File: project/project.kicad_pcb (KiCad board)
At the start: 2 copper layers, 20 x 30 mm, 10 parts, among them J1 flasher, U1 ESP32-WROOM-32

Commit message: marking version
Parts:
- removed kibuzzard-642C03EC: G***, kibuzzard-642C03EC
- added kibuzzard-64D00BC3: G***, kibuzzard-64D00BC3, F.Cu at (179.0, 116.0)

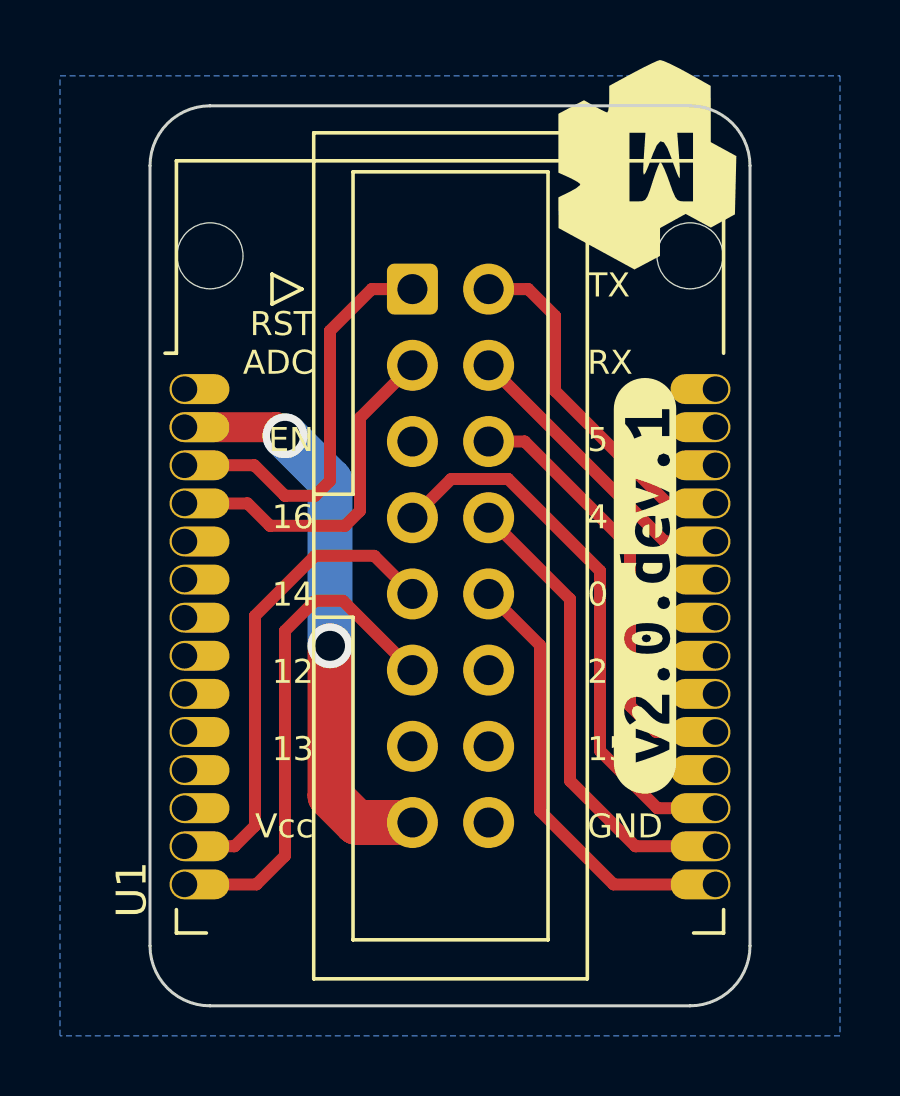
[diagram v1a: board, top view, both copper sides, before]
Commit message: using smaller 2x4 connector and shrinking pcb
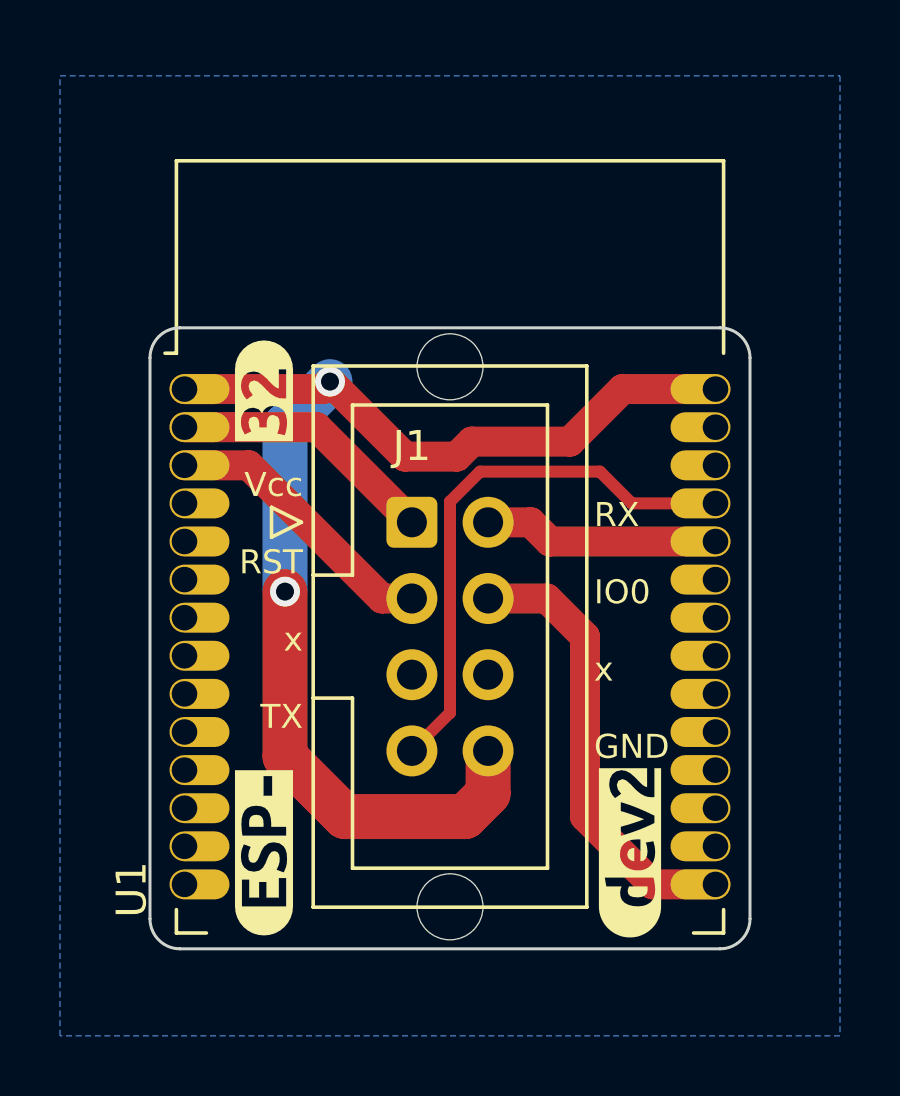
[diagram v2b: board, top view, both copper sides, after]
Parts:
- removed kibuzzard-64C972AC: G***, kibuzzard-64C972AC
- removed kibuzzard-64C97AAF: G***, kibuzzard-64C97AAF
- removed kibuzzard-64C97AF4: G***, kibuzzard-64C97AF4
- removed kibuzzard-64D00BC3: G***, kibuzzard-64D00BC3
- added kibuzzard-64DF42DF: G***, kibuzzard-64DF42DF, F.Cu at (166.3, 109.5)
- added kibuzzard-64DF42F1: G***, kibuzzard-64DF42F1, F.Cu at (166.3, 124.9)
- added kibuzzard-64DF4388: G***, kibuzzard-64DF4388, B.Cu at (177.9, 117.7)
- added kibuzzard-64DF4440: G***, kibuzzard-64DF4440, F.Cu at (178.5, 124.9)
- G2: moved to B.Cu
- J1: footprint Connector_IDC:IDC-Header_2x08_P2.54mm_Vertical -> Connector_IDC:IDC-Header_2x04_P2.54mm_Vertical
- moved G2 24.8 mm to (168.7, 124.3)
- moved REF** 23.1 mm to (172.5, 126.7)
- moved G1 16.1 mm to (168.7, 110.9)
- moved REF** 8.81 mm to (172.5, 108.7)
- moved J1 7.77 mm to (171.2, 113.9)
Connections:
- J1 pad 1: RST -> Vcc
- J1 pad 2: TX -> RX
- J1 pad 3: ADC -> RST
- J1 pad 4: RX -> IO0
- J1 pad 5: unconnected-(J1-Pad5) -> EN
- J1 pad 6: IO5 -> IO2
- J1 pad 7: IO16 -> TX
- J1 pad 8: IO4 -> GND
- U1 pad 13: IO14 -> unconnected-(U1-Pad13)
- U1 pad 14: IO12 -> unconnected-(U1-Pad14)
- U1 pad 26: IO4 -> unconnected-(U1-Pad26)
- U1 pad 27: IO16 -> unconnected-(U1-Pad27)
- U1 pad 29: IO5 -> unconnected-(U1-Pad29)
- U1 pad 4: ADC -> unconnected-(U1-Pad4)
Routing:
- net GND: track 0.00 -> 42.2 mm, vias 0 -> 2
- net IO16: track 18.7 -> 0.00 mm
- net IO12: track 16.9 -> 0.00 mm
- net IO14: track 16.2 -> 0.00 mm
- net IO4: track 15.6 -> 0.00 mm
- net IO5: track 14.7 -> 0.00 mm
- net ADC: track 11.9 -> 0.00 mm
- net Vcc: track 19.2 -> 8.89 mm, vias 2 -> 0
- net TX: track 12.0 -> 18.5 mm
- net RST: track 13.8 -> 9.42 mm
- net RX: track 9.99 -> 7.85 mm
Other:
- board size 20 x 30 mm -> 20 x 20.7 mm
- board text added: "RX IO0 x GND"
- board text added: "Vcc RST x TX"
- board text removed: "RST ADC EN 16 14 12 13 Vcc"
- board text removed: "TX RX 5 4 0 2 15 GND"

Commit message: adding 4 screwholes for mounting
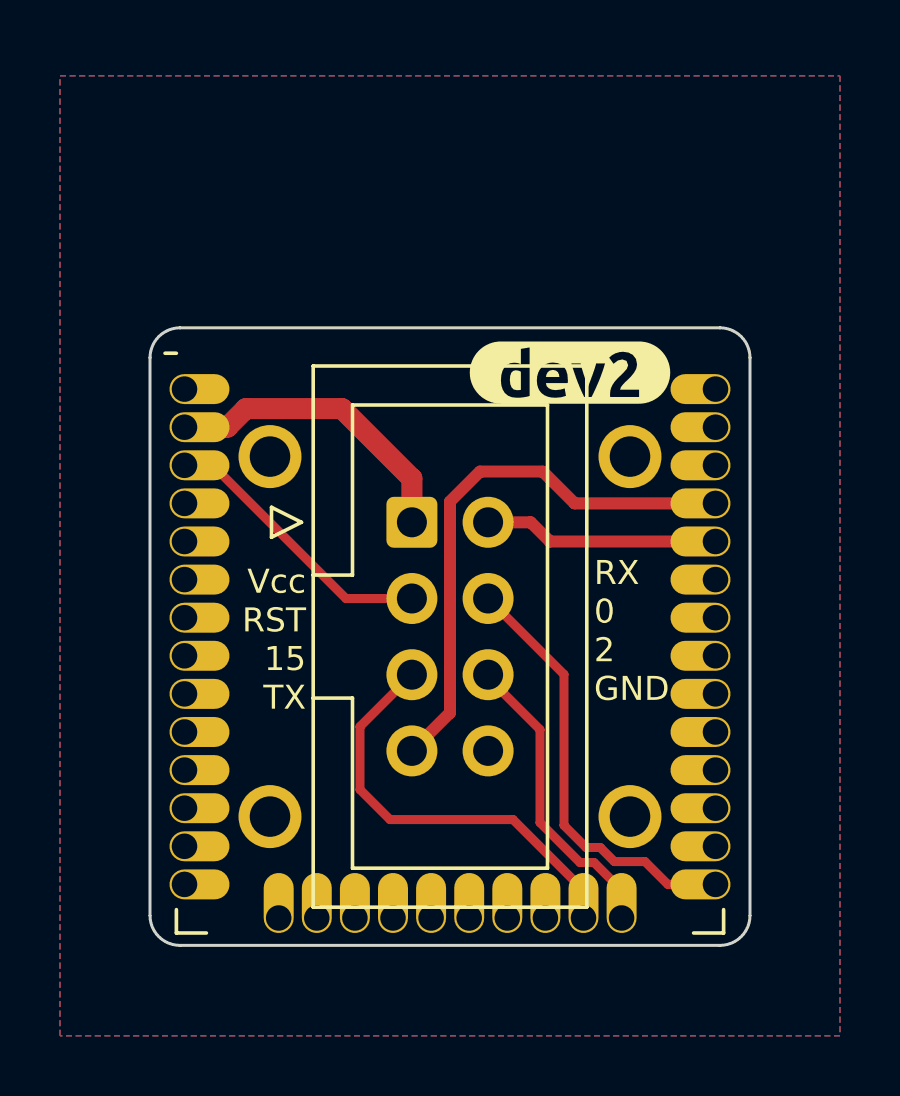
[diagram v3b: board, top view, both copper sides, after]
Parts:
- removed REF** (x2): MountingHole_2.2mm_M2, MountingHole:MountingHole_2.2mm_M2
- removed kibuzzard-64DF42DF: G***, kibuzzard-64DF42DF
- removed kibuzzard-64DF42F1: G***, kibuzzard-64DF42F1
- removed kibuzzard-64DF4440: G***, kibuzzard-64DF4440
- added H1: MountingHole_Pad, -local:MountingHole_1.35mm_M1.2_Pad, F.Cu at (166.5, 111.7)
- added H2: MountingHole_Pad, -local:MountingHole_1.35mm_M1.2_Pad, F.Cu at (178.5, 123.7)
- added H3: MountingHole_Pad, -local:MountingHole_1.35mm_M1.2_Pad, F.Cu at (178.5, 111.7)
- added H4: MountingHole_Pad, -local:MountingHole_1.35mm_M1.2_Pad, F.Cu at (166.5, 123.7)
- added kibuzzard-64E49519: G***, kibuzzard-64E49519, B.Cu at (178.6, 117.7)
- added kibuzzard-64E4955A: G***, kibuzzard-64E4955A, F.Cu at (176.5, 108.9)
- moved G1 4.21 mm to (172.9, 110.6), turned to 90 degrees
- moved G2 3.06 mm to (171.7, 123.7), turned to 90 degrees
- moved kibuzzard-64DF4388 1.74 mm to (176.3, 118.4)
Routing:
- net GND: track 42.2 -> 0.00 mm, vias 2 -> 0
- net EN: track 0.00 -> 14.3 mm
- net IO2: track 0.00 -> 10.2 mm
- net Vcc: track 8.89 -> 10.3 mm
- net IO0: track 15.0 -> 14.5 mm
- added copper zone on F.Cu, net GND
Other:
- board size 20 x 20.7 mm -> 20 x 20.6 mm
- board text added: "ESP32-WROOM-32"
- board text added: "MAKERSPACE.LT"
- board text added: "RX 0 2 GND"
- board text added: "Vcc RST 15 TX"
- board text removed: "RX IO0 x GND"
- board text removed: "Vcc RST x TX"

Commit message: added jlc silkscreen text
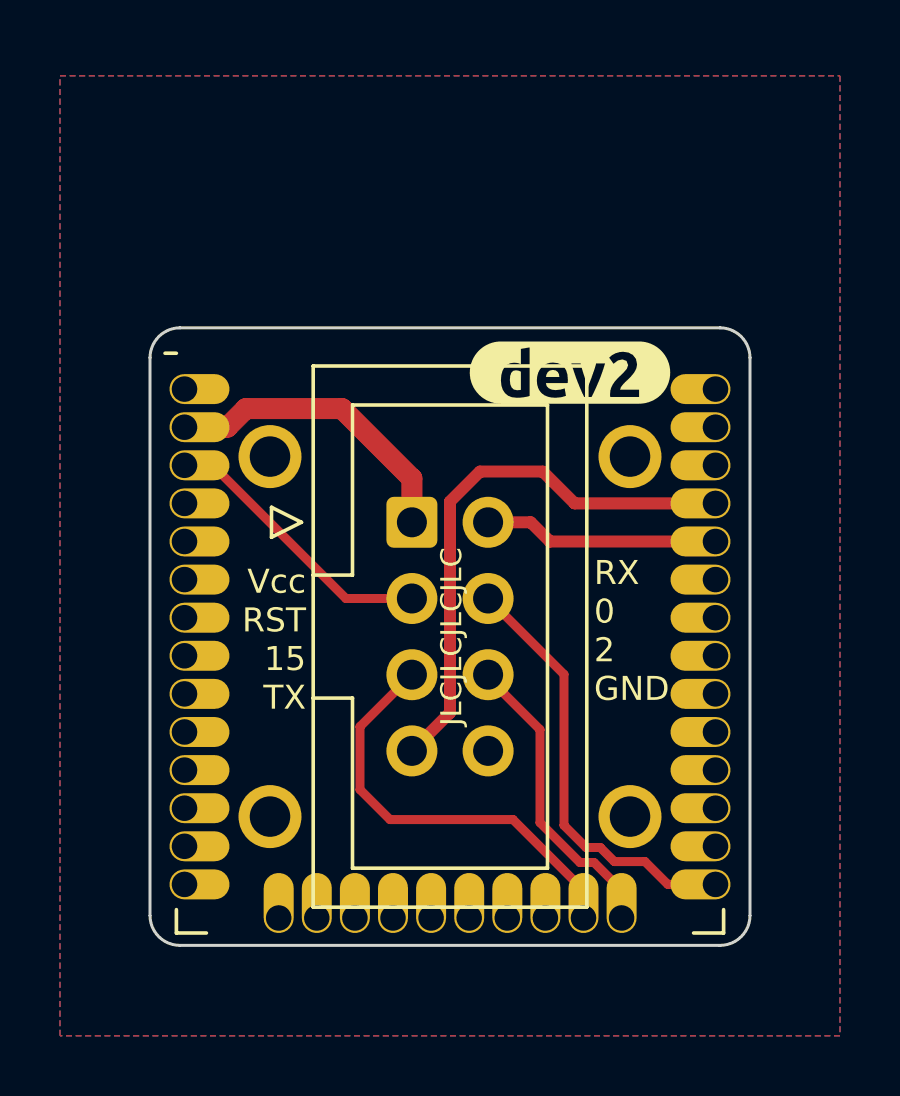
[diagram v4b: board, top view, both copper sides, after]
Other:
- board text added: "JLCJLCJLCJLC"
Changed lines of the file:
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@@
     (attr board_only exclude_from_pos_files exclude_from_bom)
     (fp_text reference "kibuzzard-64E4955A" (at 0 -4.085828) (layer "F.SilkS") hide
-      (effects (font (size 0 0)))
+      (effects (font (size 0 0) (thickness 0.15)))
     )
     (fp_text value "G***" (at 0 4.085828) (layer "F.SilkS") hide
-      (effects (font (size 0 0)))
+      (effects (font (size 0 0) (thickness 0.15)))
     )
     (fp_poly (pts
@@
     (attr board_only exclude_from_pos_files exclude_from_bom)
     (fp_text reference "kibuzzard-64E49519" (at 0 4.015581 270) (layer "B.SilkS") hide
-      (effects (font (size 0 0)) (justify mirror))
+      (effects (font (size 0 0) (thickness 0.15)) (justify mirror))
     )
     (fp_text value "G***" (at 0 -4.015581 270) (layer "B.SilkS") hide
-      (effects (font (size 0 0)) (justify mirror))
+      (effects (font (size 0 0) (thickness 0.15)) (justify mirror))
     )
     (fp_poly (pts
@@
     (effects (font (size 0.8 0.8) (thickness 0.15)) (justify right))
   )
+  (gr_text "JLCJLCJLCJLC" (at 172.55 117.6925 90) (layer "F.SilkS")
+    (effects (font (size 0.7 0.7) (thickness 0.15)))
+  )
   (gr_text "RX\n0\n2\nGND" (at 177.3 117.5) (layer "F.SilkS")
